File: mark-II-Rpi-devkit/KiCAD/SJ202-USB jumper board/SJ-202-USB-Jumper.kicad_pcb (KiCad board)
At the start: 2 copper layers, 56.2 x 26.3 mm, 3 parts, among them J1 USB_A, J2 5vJumper, J4 Conn_01x04

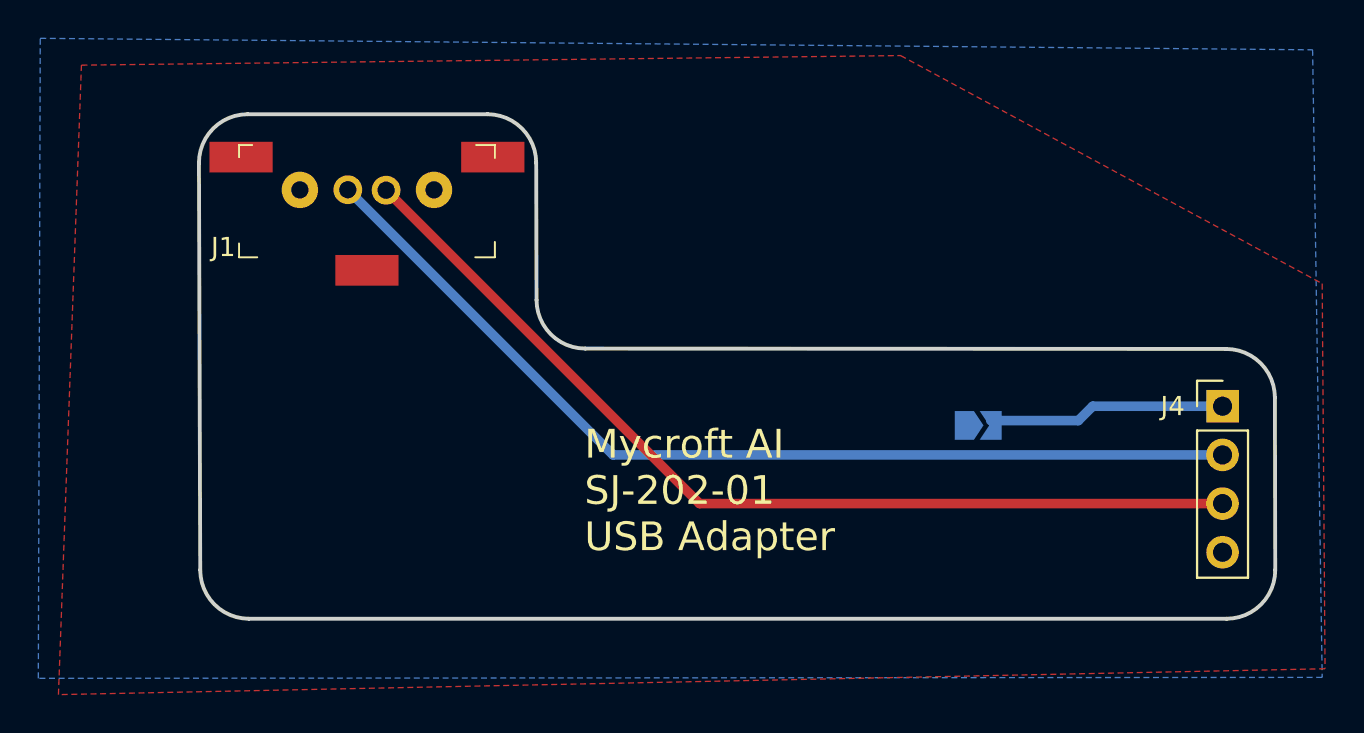
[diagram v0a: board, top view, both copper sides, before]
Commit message: SJ-201 v3, sent to PCB Fab. Removed USB Hub, add in I2S to Line Out
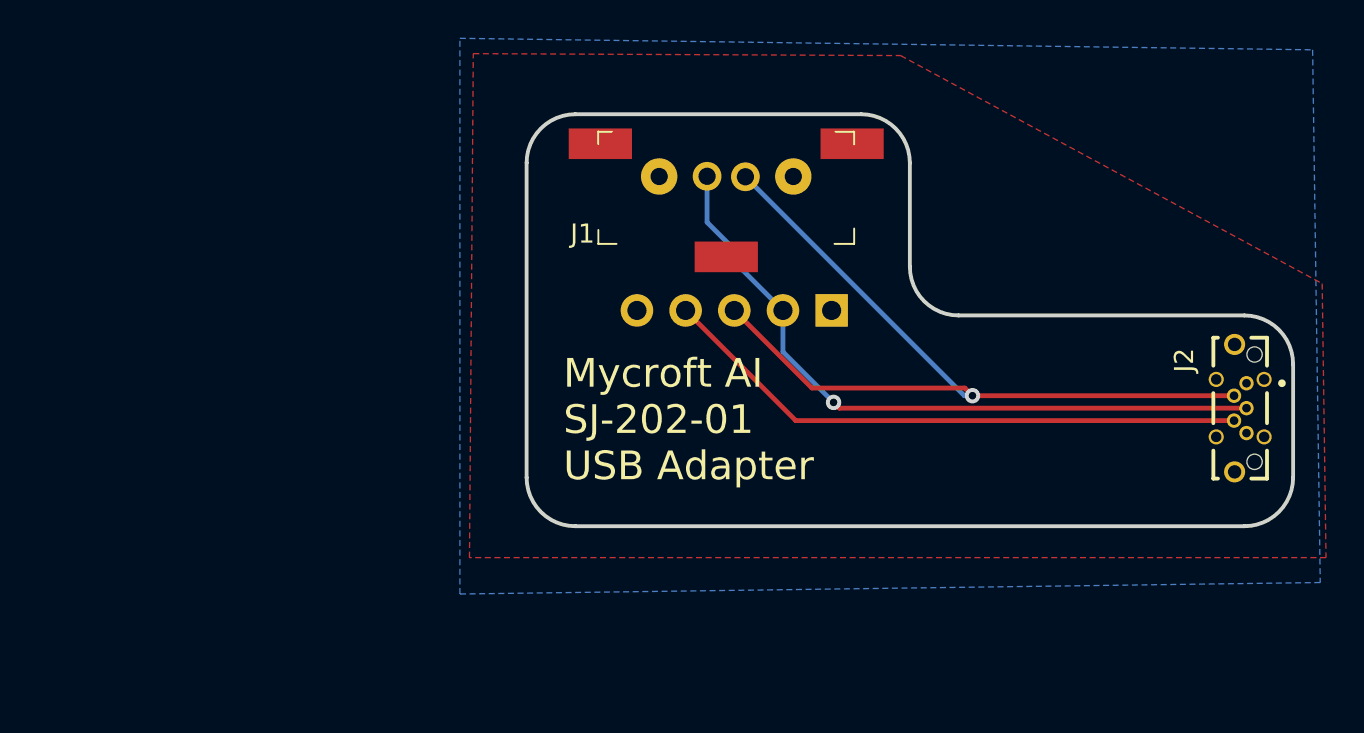
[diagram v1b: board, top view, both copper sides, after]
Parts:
- removed J4: Conn_01x04, Connector_PinHeader_2.54mm:PinHeader_1x04_P2.54mm_Vertical
- added J3: Conn_01x05, Connector_PinHeader_2.54mm:PinHeader_1x05_P2.54mm_Vertical, B.Cu at (53.9, 62.3)
- J2: value 5vJumper -> USB3150-30-130-A; footprint Jumper:SolderJumper-2_P1.3mm_Open_TrianglePad1.0x1.5mm -> libraries:GCT_USB3150-30-130-A; moved to F.Cu
- moved J1 18.8 mm to (48.4, 52.6)
- moved J2 13.4 mm to (74.9, 67.4), turned to 270 degrees
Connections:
- J2 pad 2: /5vJump -> /D-
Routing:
- net /ID: track 0.00 -> 31.1 mm, vias 0 -> 1
- net /D+: track 51.6 -> 36.2 mm, vias 0 -> 1
- net /5vJump: track 12.6 -> 0.00 mm
- net /D-: track 50.6 -> 44.5 mm, vias 0 -> 1
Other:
- board size 56.2 x 26.3 mm -> 40 x 21.5 mm
- net class Default: clearance 0.2 -> 0.1; trace_width 0.5 -> 0.25
- net class Signal Wire: clearance 0.2 -> 0.1; trace_width 0.5 -> 0.25
- rule trace_clearance: 0.2 -> 0.1
- board text added: "GND ID D- D+ 5V"
- board text removed: "5V D+ D- GND"

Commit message: SJ-202 USB Jumper Update & Readme updates
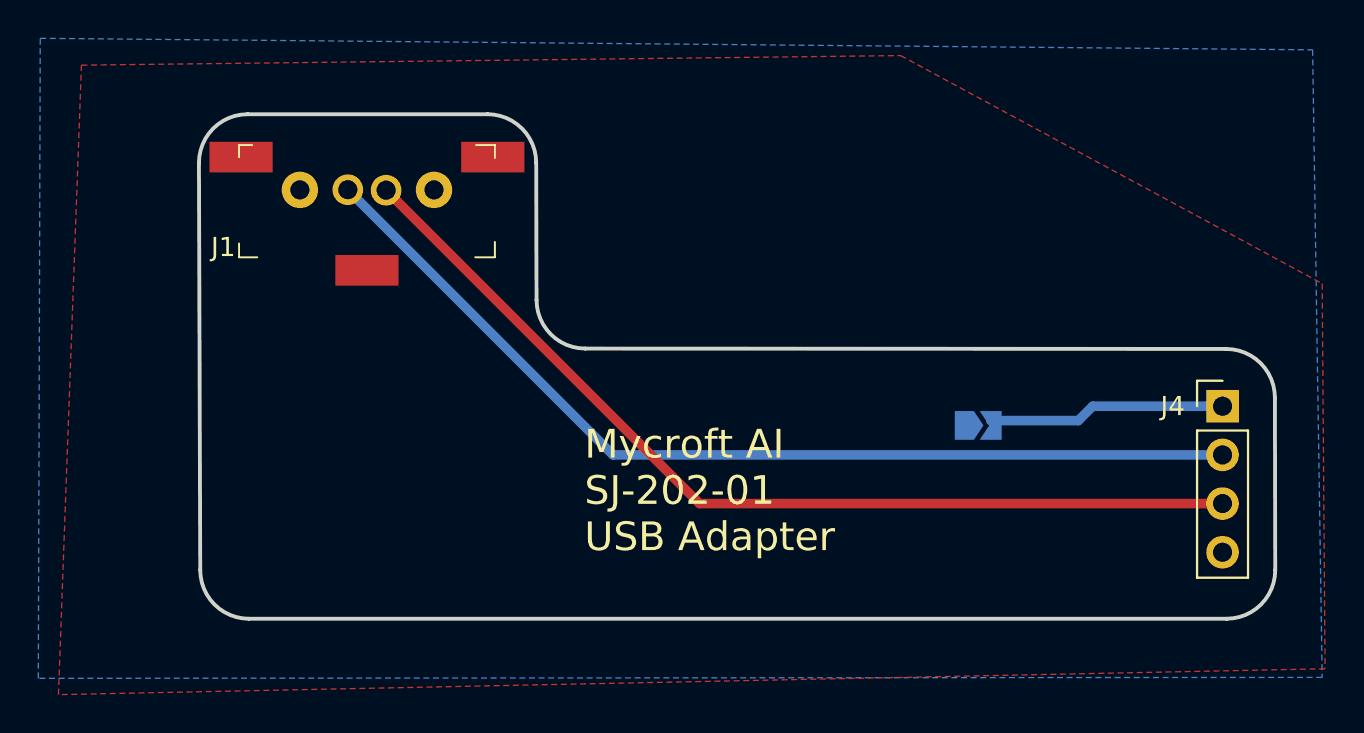
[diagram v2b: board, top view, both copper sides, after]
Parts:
- removed J3: Conn_01x05, Connector_PinHeader_2.54mm:PinHeader_1x05_P2.54mm_Vertical
- added J4: Conn_01x04, Connector_PinHeader_2.54mm:PinHeader_1x04_P2.54mm_Vertical, F.Cu at (74.3, 67.3)
- J2: value USB3150-30-130-A -> 5vJumper; footprint libraries:GCT_USB3150-30-130-A -> Jumper:SolderJumper-2_P1.3mm_Open_TrianglePad1.0x1.5mm; moved to B.Cu
- moved J1 18.8 mm to (29.6, 53.3)
- moved J2 13.4 mm to (61.5, 68.3), turned to 0 degrees
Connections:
- J2 pad 2: /D- -> /5vJump
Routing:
- net /ID: track 31.1 -> 0.00 mm, vias 1 -> 0
- net /D+: track 36.2 -> 51.6 mm, vias 1 -> 0
- net /5vJump: track 0.00 -> 12.6 mm
- net /D-: track 44.5 -> 50.6 mm, vias 1 -> 0
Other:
- board size 40 x 21.5 mm -> 56.2 x 26.3 mm
- net class Default: clearance 0.1 -> 0.2; trace_width 0.25 -> 0.5
- net class Signal Wire: clearance 0.1 -> 0.2; trace_width 0.25 -> 0.5
- rule trace_clearance: 0.1 -> 0.2
- board text added: "5V D+ D- GND"
- board text removed: "GND ID D- D+ 5V"
